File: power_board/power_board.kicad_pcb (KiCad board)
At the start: 2 copper layers, 163.7 x 117.7 mm, 82 parts, among them J1 PROG, J10 M4, J11 5V_1, J12 M5, J13 M6, J14 M7, J15 FAN, J16 Screw_Terminal_01x02, J17 MB_interface, J18 Conn_01x02_Female, J19 12V_1, J2 M1, J20 12V_2, J21 12V_3, J22 12V_4, J23 48V_1, J24 48V_2, J25 48V_3, J26 48V_4, J27 Screw_Terminal_01x02, J3 M2, J4 Conn_01x02_Female, J5 Conn_01x02_Female, J6 Conn_01x01_Male, J7 Conn_01x01_Male, J8 Screw_Terminal_01x02, J9 M3, Q1 2N3906, SW1 SW_Push, U1 ACS758xCB-050B-PFF, U10 MAX31855KASA, U2 ACS758xCB-050B-PFF, U3 MCP2515-EST, U4 MAX31855KASA, U5 ATA6560,1, U6 BTS50085-1TMA, U7 ATmega328P-AU, U8 BTS50085-1TMA, U9 LM2596S-5, Y1 20Mhz, Y2 16Mhz

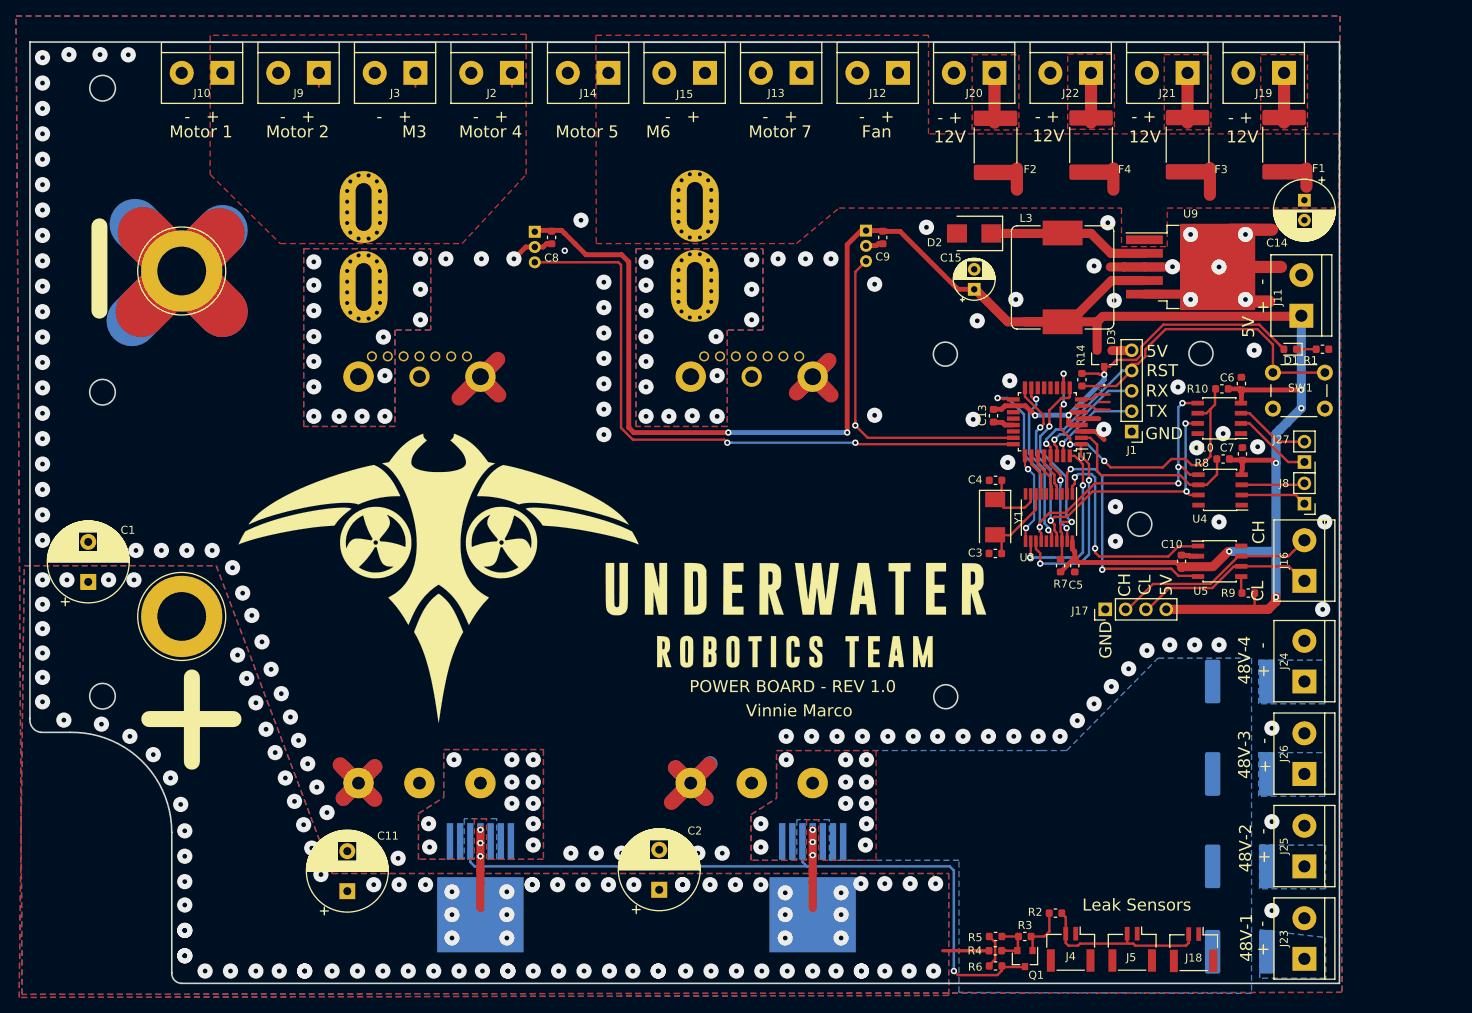
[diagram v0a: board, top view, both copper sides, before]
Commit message: Added new mouting holes for right hand side of pcb
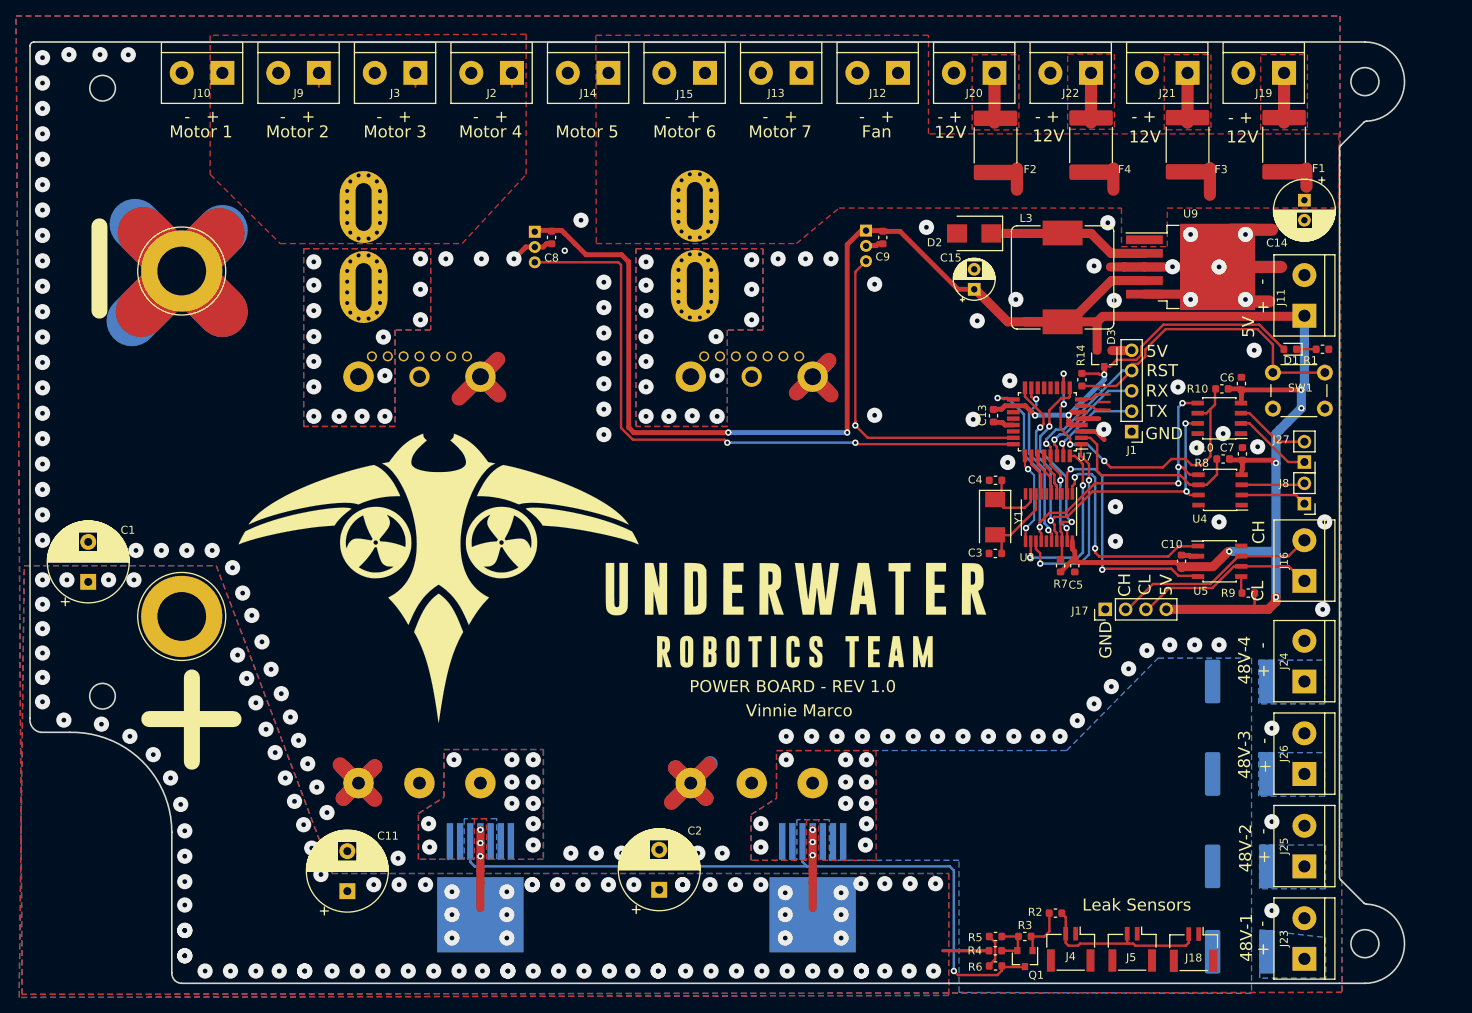
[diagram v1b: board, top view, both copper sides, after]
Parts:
- moved J11 0.38 mm to (221.6, 66.5)
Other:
- board size 163.7 x 117.7 mm -> 171.8 x 117.7 mm
- board text added: "Motor 3"
- board text added: "Motor 6"
- board text removed: "M3"
- board text removed: "M6"
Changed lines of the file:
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@@
   (general
     (thickness 1.6)
-    (drawings 67)
-    (tracks 861)
+    (drawings 73)
+    (tracks 863)
     (zones 0)
     (modules 82)
@@
   )
   (module TerminalBlock:TerminalBlock_bornier-2_P5.08mm (layer F.Cu)
-    (at 221.234 66.548 90)
+    (at 221.615 66.548 90)
     (descr "simple 2-pin terminal block, pitch 5.08mm, revamped version of bornier2")
     (tags "terminal block bornier2")
@@
       (xy -13.727278 2.362363) (xy -13.654921 2.345019) (xy -13.369211 2.320423) (xy -13.110773 2.36591)) (layer F.SilkS) (width 0.01))
   )
-  (gr_line (start 81.228701 150.002699) (end 225.996515 150.002699) (layer Edge.Cuts) (width 0.2))
-  (gr_line (start 225.996515 150.002699) (end 225.996515 37.290199) (layer Edge.Cuts) (width 0.2))
+  (gr_circle (center 229.180248 37.285694) (end 230.930248 37.285694) (layer Edge.Cuts) (width 0.2))
+  (gr_arc (start 63.869585 117.072557) (end 62.318197 116.888994) (angle -90) (layer Edge.Cuts) (width 0.2))
+  (gr_arc (start 229.180248 145.04529) (end 229.180248 149.998194) (angle -177.7803021) (layer Edge.Cuts) (width 0.2))
+  (gr_arc (start 229.180248 37.285694) (end 229.37208 42.234881) (angle -177.7803021) (layer Edge.Cuts) (width 0.2))
+  (gr_arc (start 81.302683 148.739644) (end 80.044133 148.674395) (angle -89.99999988) (layer Edge.Cuts) (width 0.2))
+  (gr_arc (start 226.505248 136.710279) (end 226.005248 136.710279) (angle -45) (layer Edge.Cuts) (width 0.2))
+  (gr_line (start 80.043854 131.109174) (end 80.044133 148.674395) (layer Edge.Cuts) (width 0.2))
+  (gr_arc (start 229.391446 42.734506) (end 229.37208 42.234881) (angle -42.78030211) (layer Edge.Cuts) (width 0.2))
+  (gr_line (start 62.318197 32.83279) (end 62.318197 116.888994) (layer Edge.Cuts) (width 0.2))
+  (gr_line (start 226.005248 149.998194) (end 229.180248 149.998194) (layer Edge.Cuts) (width 0.2))
+  (gr_arc (start 229.391446 139.596477) (end 229.037892 139.950031) (angle -42.78030211) (layer Edge.Cuts) (width 0.2))
+  (gr_line (start 62.818197 32.33279) (end 229.180248 32.33279) (layer Edge.Cuts) (width 0.2))
+  (gr_line (start 229.037892 42.380953) (end 226.151694 45.267151) (layer Edge.Cuts) (width 0.2))
+  (gr_arc (start 62.818197 32.83279) (end 62.818197 32.33279) (angle -90) (layer Edge.Cuts) (width 0.2))
+  (gr_line (start 63.686022 118.623945) (end 67.299777 118.623945) (layer Edge.Cuts) (width 0.2))
+  (gr_arc (start 226.505248 45.620705) (end 226.151694 45.267151) (angle -45) (layer Edge.Cuts) (width 0.2))
+  (gr_line (start 81.237434 149.998194) (end 226.005248 149.998194) (layer Edge.Cuts) (width 0.2))
+  (gr_line (start 226.005248 136.710279) (end 226.005248 45.620705) (layer Edge.Cuts) (width 0.2))
+  (gr_line (start 229.037892 139.950031) (end 226.151694 137.063832) (layer Edge.Cuts) (width 0.2))
+  (gr_circle (center 229.180248 145.04529) (end 230.930248 145.04529) (layer Edge.Cuts) (width 0.2))
+  (gr_arc (start 67.555997 131.109174) (end 80.043854 131.109174) (angle -91.17565039) (layer Edge.Cuts) (width 0.2))
+  (gr_circle (center 71.38887 38.107527) (end 69.78887 38.107527) (layer Edge.Cuts) (width 0.2))
   (gr_circle (center 71.377739 114.108975) (end 69.777739 114.108975) (layer Edge.Cuts) (width 0.2))
-  (gr_circle (center 71.377739 76.108975) (end 69.777739 76.108975) (layer Edge.Cuts) (width 0.2))
-  (gr_line (start 63.677289 118.62845) (end 67.291044 118.62845) (layer Edge.Cuts) (width 0.2))
-  (gr_arc (start 63.860852 117.077062) (end 62.309464 116.893499) (angle -90) (layer Edge.Cuts) (width 0.2))
-  (gr_line (start 62.309464 32.337295) (end 225.996515 32.337295) (layer Edge.Cuts) (width 0.2))
-  (gr_line (start 225.996515 37.290199) (end 225.996515 32.337295) (layer Edge.Cuts) (width 0.2))
-  (gr_arc (start 67.547264 131.113679) (end 80.035121 131.113679) (angle -91.17564804) (layer Edge.Cuts) (width 0.2))
-  (gr_line (start 62.309464 116.893499) (end 62.309464 32.337295) (layer Edge.Cuts) (width 0.2))
-  (gr_arc (start 81.29395 148.744149) (end 80.0354 148.6789) (angle -89.99999988) (layer Edge.Cuts) (width 0.2))
-  (gr_line (start 80.0354 148.6789) (end 80.035121 131.113679) (layer Edge.Cuts) (width 0.2))
   (gr_text "Vinnie Marco" (at 158.4706 115.9256) (layer F.SilkS)
     (effects (font (size 1.5 1.5) (thickness 0.3)))
@@
     (effects (font (size 1.5 1.5) (thickness 0.375)))
   )
-  (gr_circle (center 208.685 71.2724) (end 207.185 71.2724) (layer Edge.Cuts) (width 0.2))
-  (gr_circle (center 71.38887 38.107527) (end 69.78887 38.107527) (layer Edge.Cuts) (width 0.2))
-  (gr_circle (center 176.784 114.173) (end 175.284 114.173) (layer Edge.Cuts) (width 0.2))
-  (gr_circle (center 176.7332 71.3486) (end 175.2332 71.3486) (layer Edge.Cuts) (width 0.2))
-  (gr_circle (center 201.041 92.607) (end 199.541 92.607) (layer Edge.Cuts) (width 0.2))
   (gr_line (start 70.993 65.913) (end 70.993 55.372) (layer F.SilkS) (width 2))
   (gr_line (start 77.216 116.967) (end 87.757 116.967) (layer F.SilkS) (width 2))
@@
     (effects (font (size 1.5 1.5) (thickness 0.375)))
   )
-  (gr_text 12V (at 177.292 44.196) (layer F.SilkS)
+  (gr_text 12V (at 177.3682 43.6118) (layer F.SilkS)
     (effects (font (size 1.5 1.5) (thickness 0.375)))
   )
@@
     (effects (font (size 1.5 1.5) (thickness 0.375)))
   )
-  (gr_text M6 (at 140.843 43.561) (layer F.SilkS)
+  (gr_text "Motor 6" (at 144.145 43.561) (layer F.SilkS)
     (effects (font (size 1.5 1.5) (thickness 0.375)))
   )
@@
     (effects (font (size 1.5 1.5) (thickness 0.375)))
   )
-  (gr_text M3 (at 110.363 43.561) (layer F.SilkS)
+  (gr_text "Motor 3" (at 107.95 43.561) (layer F.SilkS)
     (effects (font (size 1.5 1.5) (thickness 0.375)))
   )
@@
     (effects (font (size 1.5 1.5) (thickness 0.375)))
   )
-  (gr_text "- +" (at 177.292 41.783) (layer F.SilkS)
+  (gr_text "- +" (at 177.292 41.6814) (layer F.SilkS)
     (effects (font (size 1.5 1.5) (thickness 0.375)))
   )
@@
   (segment (start 213.741 75.819) (end 213.741 76.3565) (width 0.6096) (layer F.Cu) (net 3))
   (segment (start 213.741 76.3565) (end 213.741 77.47) (width 0.6096) (layer F.Cu) (net 3))
-  (via (at 221.234 75.819) (size 0.8) (drill 0.4) (layers F.Cu B.Cu) (net 3))
-  (segment (start 213.741 75.819) (end 221.234 75.819) (width 0.6096) (layer F.Cu) (net 3))
-  (segment (start 221.234 66.548) (end 221.234 75.819) (width 1.143) (layer B.Cu) (net 3))
-  (segment (start 221.234 78.105) (end 221.234 75.819) (width 1.143) (layer B.Cu) (net 3))
   (segment (start 212.09 75.692) (end 213.614 75.692) (width 0.6096) (layer F.Cu) (net 3))
   (segment (start 213.614 75.692) (end 213.741 75.819) (width 0.6096) (layer F.Cu) (net 3))
@@
   (segment (start 196.393499 66.623501) (end 195.707 67.31) (width 1.143) (layer F.Cu) (net 3))
   (segment (start 196.544501 66.623501) (end 196.393499 66.623501) (width 0.6096) (layer F.Cu) (net 3))
+  (segment (start 213.741 75.819) (end 221.234 75.819) (width 0.6096) (layer F.Cu) (net 3))
+  (segment (start 221.234 78.105) (end 221.234 75.819) (width 1.143) (layer B.Cu) (net 3))
+  (segment (start 221.234 66.548) (end 221.615 66.929) (width 1.143) (layer B.Cu) (net 3))
+  (segment (start 221.615 66.929) (end 221.615 75.438) (width 1.143) (layer B.Cu) (net 3))
+  (segment (start 221.615 75.438) (end 221.234 75.819) (width 1.143) (layer B.Cu) (net 3))
+  (via (at 221.234 75.819) (size 0.8) (drill 0.4) (layers F.Cu B.Cu) (net 3) (status 1000000))
   (via (at 165.481 80.264) (size 0.8) (drill 0.4) (layers F.Cu B.Cu) (net 4))
   (segment (start 167.027 81.81) (end 165.481 80.264) (width 0.3048) (layer F.Cu) (net 4))

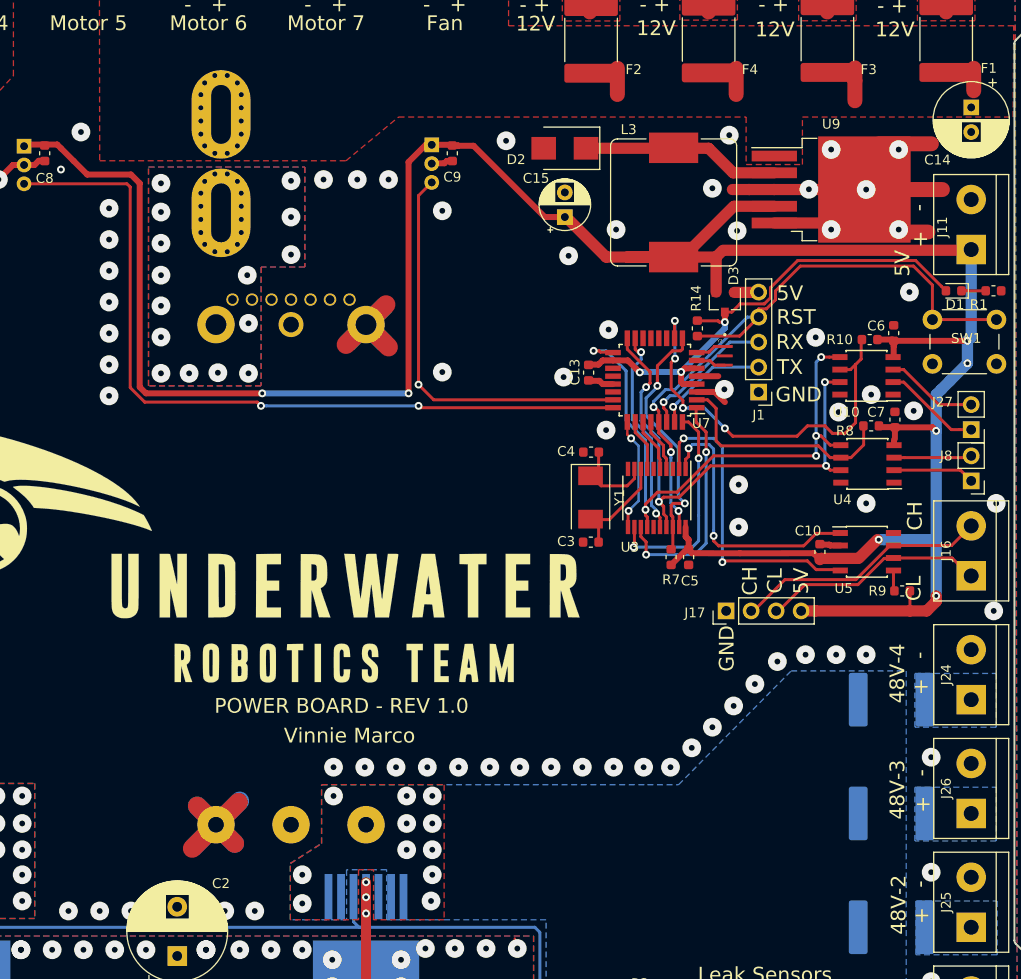
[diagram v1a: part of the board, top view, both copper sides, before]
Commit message: added new mounting holes for main board
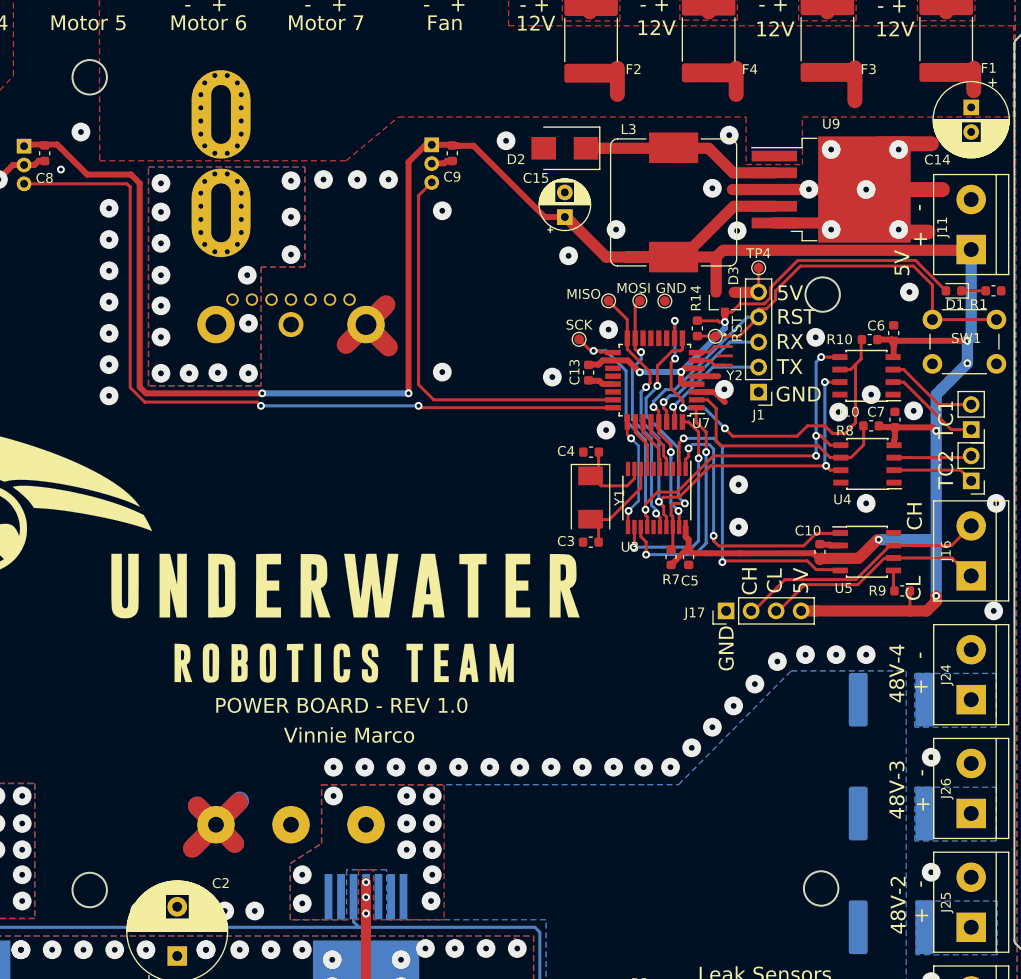
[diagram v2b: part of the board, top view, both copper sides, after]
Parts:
- added GND: GND, TestPoint:TestPoint_Pad_D1.0mm, F.Cu at (190.5, 71.8)
- added MISO: MISO, TestPoint:TestPoint_Pad_D1.0mm, F.Cu at (184.8, 71.8)
- added MOSI: MOSI, TestPoint:TestPoint_Pad_D1.0mm, F.Cu at (188.0, 71.8)
- added RST: RST, TestPoint:TestPoint_Pad_D1.0mm, F.Cu at (195.6, 75.4)
- added SCK: SCK, TestPoint:TestPoint_Pad_D1.0mm, F.Cu at (181.8, 75.7)
- added TP4: +5V, TestPoint:TestPoint_Pad_D1.0mm, F.Cu at (200.0, 68.4)
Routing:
- net MISO: track 51.8 -> 56.4 mm
- net MOSI: track 21.1 -> 25.1 mm
- net VPP: track 2.49 -> 4.78 mm
- net SCK: track 58.0 -> 60.0 mm
- net GNDREF: vias 113 -> 111
- net 12VA_SENSE: vias 1 -> 0
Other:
- outline, holes or cut-outs redrawn
- board text added: "TC1"
- board text added: "TC2"
